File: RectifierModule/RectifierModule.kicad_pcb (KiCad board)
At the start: 2 copper layers, 45 x 70 mm, 20 parts, among them J1 TransformerIn, J2 Rectified Out, J3 AuxIn, J4 VA, J5 FAN, J6 Extra, U1 LM7812_TO220

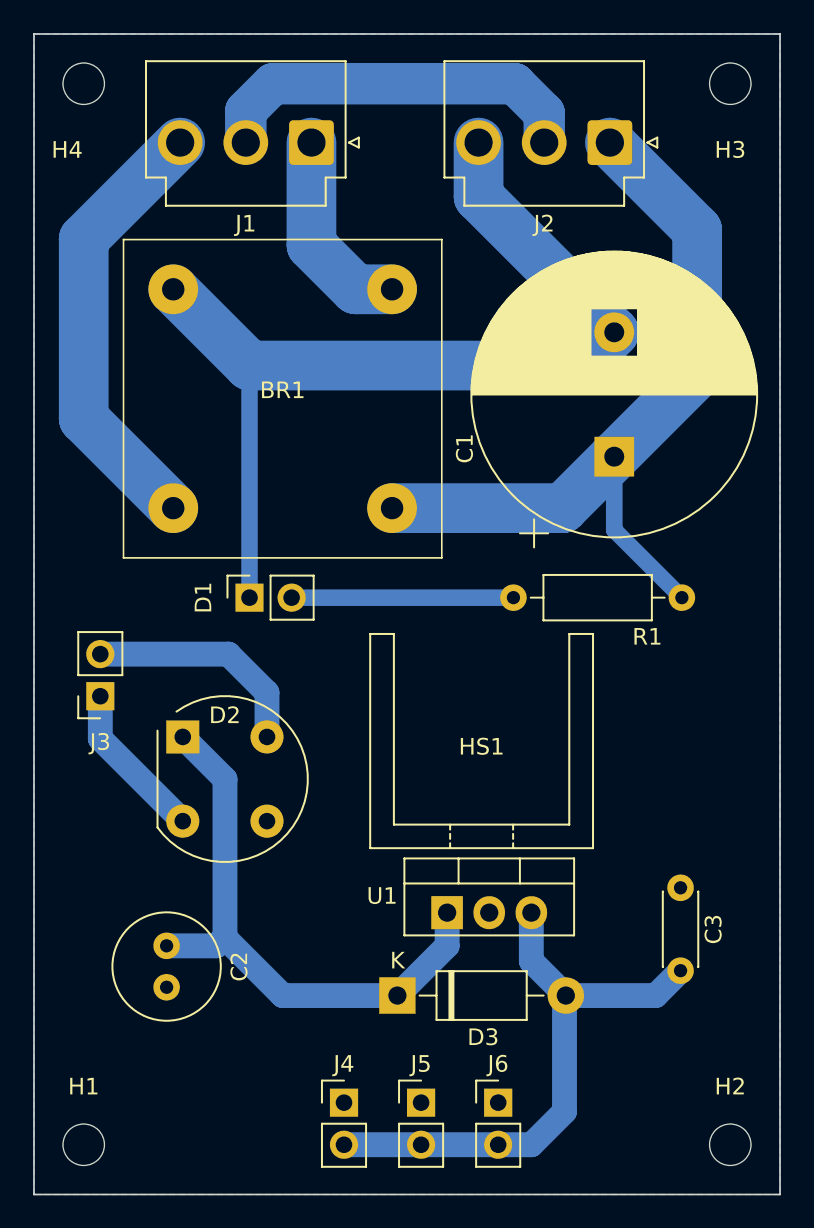
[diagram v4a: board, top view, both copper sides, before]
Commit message: Curved tracks in pcb and BOM
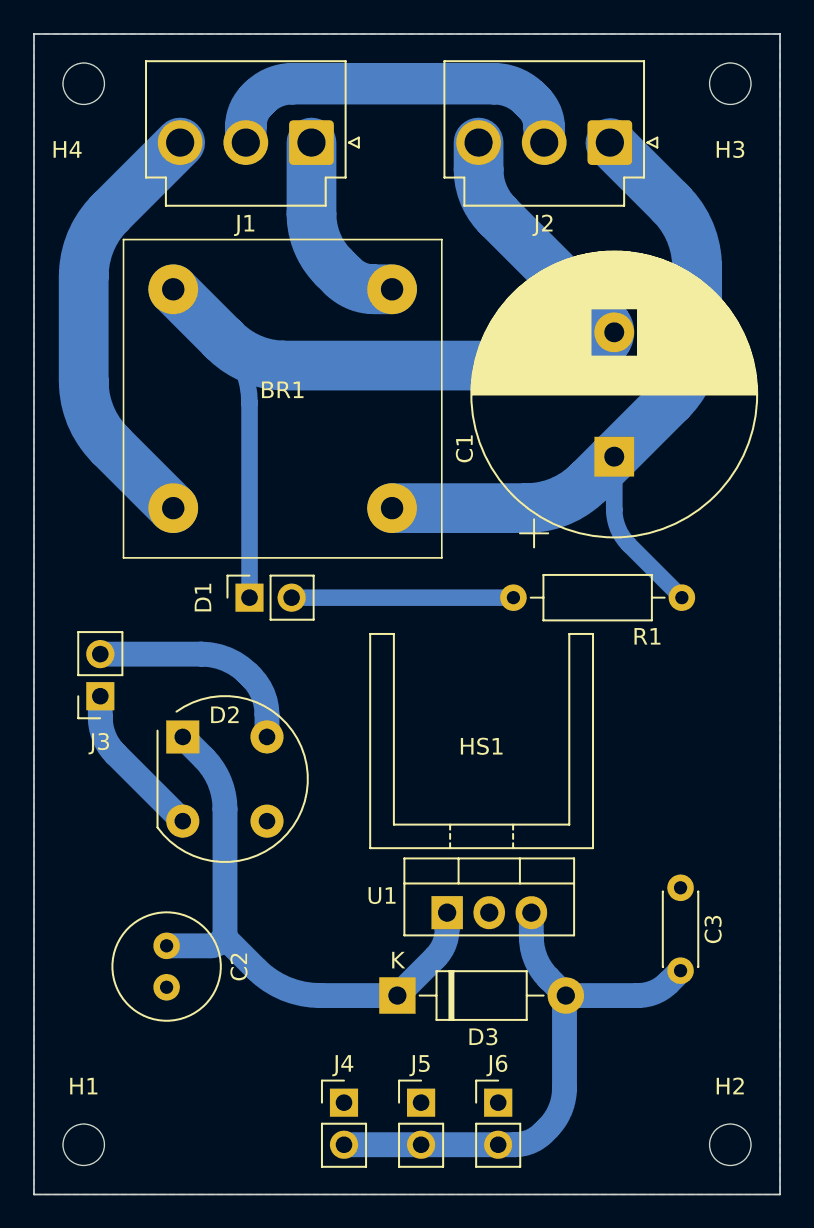
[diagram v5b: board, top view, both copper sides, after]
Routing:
- net /30V-: track 58.2 -> 59.2 mm
- net /30V+: track 48.2 -> 47.2 mm
- net /12V+: track 35.0 -> 34.4 mm
- net /AC_IN_L: track 26.7 -> 26.2 mm
